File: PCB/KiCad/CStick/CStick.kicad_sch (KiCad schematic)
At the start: 6 parts, among them J1 Conn_01x04_Male, U1 Stickbox_Assembly

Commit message: 1.2.2 overhaul
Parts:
- added H5, H6: MouseBite, PhobGCC_Footprints:breakaway-mousebites-double, symbol Mechanical:MountingHole
- H1: footprint (none) -> PhobGCC_Footprints:MountingHole_1.8mm
- H2: footprint (none) -> PhobGCC_Footprints:MountingHole_5.2mm
- H3, H4: footprint (none) -> PhobGCC_Footprints:MountingHole_2.0mm
- U1: footprint (none) -> PhobGCC_Footprints:GCC_Stickbox_Hall_Only
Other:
- moved on the sheet: H1, H2, H3, H4, J1, U1

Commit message: Consolidated footprints to PhobGCC library
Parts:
- J1: footprint Connector_PinHeader_2.00mm:PinHeader_1x04_P2.00mm_Vertical -> (none)
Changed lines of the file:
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@@
     (property "Reference" "J1" (id 0) (at 44.577 32.2793 0))
     (property "Value" "Conn_01x04_Male" (id 1) (at 44.577 35.0544 0))
-    (property "Footprint" "Connector_PinHeader_2.00mm:PinHeader_1x04_P2.00mm_Vertical" (id 2) (at 43.942 38.862 0)
+    (property "Footprint" "" (id 2) (at 43.942 38.862 0)
       (effects (font (size 1.27 1.27)) hide)
     )
@@
     )
     (path "/61d7b681-5321-4eb3-aa94-2064a3bbd361"
-      (reference "J1") (unit 1) (value "Conn_01x04_Male") (footprint "Connector_PinHeader_2.00mm:PinHeader_1x04_P2.00mm_Vertical")
+      (reference "J1") (unit 1) (value "Conn_01x04_Male") (footprint "PhobGCC_Footprints:PinHeader_1x04_P2.00mm_Vertical")
     )
     (path "/8ae1c09a-53cf-4ff3-980c-45e96b7744a8"

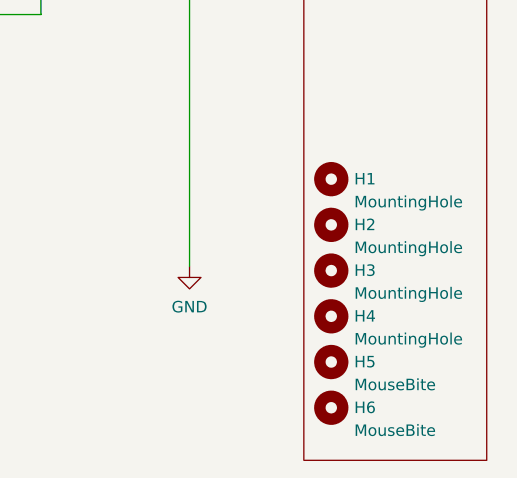
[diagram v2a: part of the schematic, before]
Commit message: 1.2.3 changes
omron tactile z support, larger c stick pin holes, relocated C10 from underneath button pad
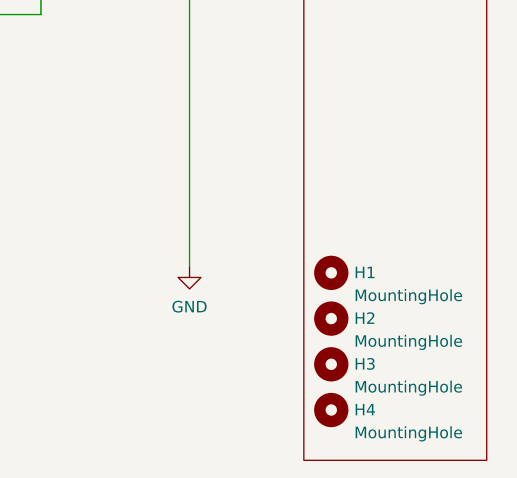
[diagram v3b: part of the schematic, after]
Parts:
- removed H5, H6: MouseBite, PhobGCC_Footprints:breakaway-mousebites-double, symbol Mechanical:MountingHole
- J1: footprint (none) -> PhobGCC_Footprints:PinHeader_1x04_P2.00mm_Vertical
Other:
- moved on the sheet: H1, H2, H3, H4
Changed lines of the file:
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@@
     (pin "1")
   )
-  (symbol (lib_id "Mechanical:MountingHole") (at 104.14 76.2 0) (unit 1)
+  (symbol (lib_id "Mechanical:MountingHole") (at 104.14 86.614 0) (unit 1)
     (in_bom yes) (on_board yes)
-    (property "Reference" "H3" (id 0) (at 106.68 76.2 0)
+    (property "Reference" "H3" (id 0) (at 106.68 86.614 0)
       (effects (font (size 1.27 1.27)) (justify left))
     )
-    (property "Value" "MountingHole" (id 1) (at 106.68 78.74 0)
+    (property "Value" "MountingHole" (id 1) (at 106.68 89.154 0)
       (effects (font (size 1.27 1.27)) (justify left))
     )
-    (property "Footprint" "PhobGCC_Footprints:MountingHole_2.0mm" (id 2) (at 104.14 76.2 0)
+    (property "Footprint" "PhobGCC_Footprints:MountingHole_2.0mm" (id 2) (at 104.14 86.614 0)
       (effects (font (size 1.27 1.27)) hide)
     )
-    (property "Datasheet" "~" (id 3) (at 104.14 76.2 0)
+    (property "Datasheet" "~" (id 3) (at 104.14 86.614 0)
       (effects (font (size 1.27 1.27)) hide)
     )
@@
     (pin "1")
   )
-  (symbol (lib_id "Mechanical:MountingHole") (at 104.14 81.28 0) (unit 1)
+  (symbol (lib_id "Mechanical:MountingHole") (at 104.14 91.694 0) (unit 1)
     (in_bom yes) (on_board yes)
-    (property "Reference" "H4" (id 0) (at 106.68 81.28 0)
+    (property "Reference" "H4" (id 0) (at 106.68 91.694 0)
       (effects (font (size 1.27 1.27)) (justify left))
     )
-    (property "Value" "MountingHole" (id 1) (at 106.68 83.82 0)
+    (property "Value" "MountingHole" (id 1) (at 106.68 94.234 0)
       (effects (font (size 1.27 1.27)) (justify left))
     )
-    (property "Footprint" "PhobGCC_Footprints:MountingHole_2.0mm" (id 2) (at 104.14 81.28 0)
+    (property "Footprint" "PhobGCC_Footprints:MountingHole_2.0mm" (id 2) (at 104.14 91.694 0)
       (effects (font (size 1.27 1.27)) hide)
     )
-    (property "Datasheet" "~" (id 3) (at 104.14 81.28 0)
+    (property "Datasheet" "~" (id 3) (at 104.14 91.694 0)
       (effects (font (size 1.27 1.27)) hide)
     )
@@
     (property "Reference" "J1" (id 0) (at 44.577 32.2793 0))
     (property "Value" "Conn_01x04_Male" (id 1) (at 44.577 35.0544 0))
-    (property "Footprint" "" (id 2) (at 43.942 38.862 0)
+    (property "Footprint" "PhobGCC_Footprints:PinHeader_1x04_P2.00mm_Vertical" (id 2) (at 43.942 38.862 0)
       (effects (font (size 1.27 1.27)) hide)
     )
@@
     (pin "1")
   )
-  (symbol (lib_id "Mechanical:MountingHole") (at 104.14 86.36 0) (unit 1)
+  (symbol (lib_id "Mechanical:MountingHole") (at 104.14 81.534 0) (unit 1)
     (in_bom yes) (on_board yes)
-    (property "Reference" "H5" (id 0) (at 106.68 86.36 0)
+    (property "Reference" "H2" (id 0) (at 106.68 81.534 0)
       (effects (font (size 1.27 1.27)) (justify left))
     )
-    (property "Value" "MouseBite" (id 1) (at 106.68 88.9 0)
+    (property "Value" "MountingHole" (id 1) (at 106.68 84.074 0)
       (effects (font (size 1.27 1.27)) (justify left))
     )
-    (property "Footprint" "PhobGCC_Footprints:breakaway-mousebites-double" (id 2) (at 104.14 86.36 0)
+    (property "Footprint" "PhobGCC_Footprints:MountingHole_5.2mm" (id 2) (at 104.14 81.534 0)
       (effects (font (size 1.27 1.27)) hide)
     )
-    (property "Datasheet" "~" (id 3) (at 104.14 86.36 0)
+    (property "Datasheet" "~" (id 3) (at 104.14 81.534 0)
       (effects (font (size 1.27 1.27)) hide)
     )
   )
-  (symbol (lib_id "Mechanical:MountingHole") (at 104.14 71.12 0) (unit 1)
+  (symbol (lib_id "Mechanical:MountingHole") (at 104.14 76.454 0) (unit 1)
     (in_bom yes) (on_board yes)
-    (property "Reference" "H2" (id 0) (at 106.68 71.12 0)
+    (property "Reference" "H1" (id 0) (at 106.68 76.454 0)
       (effects (font (size 1.27 1.27)) (justify left))
     )
-    (property "Value" "MountingHole" (id 1) (at 106.68 73.66 0)
+    (property "Value" "MountingHole" (id 1) (at 106.68 78.994 0)
       (effects (font (size 1.27 1.27)) (justify left))
     )
-    (property "Footprint" "PhobGCC_Footprints:MountingHole_5.2mm" (id 2) (at 104.14 71.12 0)
+    (property "Footprint" "PhobGCC_Footprints:MountingHole_1.8mm" (id 2) (at 104.14 76.454 0)
       (effects (font (size 1.27 1.27)) hide)
     )
-    (property "Datasheet" "~" (id 3) (at 104.14 71.12 0)
-      (effects (font (size 1.27 1.27)) hide)
-    )
-  )
-  (symbol (lib_id "Mechanical:MountingHole") (at 104.14 91.44 0) (unit 1)
-    (in_bom yes) (on_board yes)
-    (property "Reference" "H6" (id 0) (at 106.68 91.44 0)
-      (effects (font (size 1.27 1.27)) (justify left))
-    )
-    (property "Value" "MouseBite" (id 1) (at 106.68 93.98 0)
-      (effects (font (size 1.27 1.27)) (justify left))
-    )
-    (property "Footprint" "PhobGCC_Footprints:breakaway-mousebites-double" (id 2) (at 104.14 91.44 0)
-      (effects (font (size 1.27 1.27)) hide)
-    )
-    (property "Datasheet" "~" (id 3) (at 104.14 91.44 0)
-      (effects (font (size 1.27 1.27)) hide)
-    )
-  )
-  (symbol (lib_id "Mechanical:MountingHole") (at 104.14 66.04 0) (unit 1)
-    (in_bom yes) (on_board yes)
-    (property "Reference" "H1" (id 0) (at 106.68 66.04 0)
-      (effects (font (size 1.27 1.27)) (justify left))
-    )
-    (property "Value" "MountingHole" (id 1) (at 106.68 68.58 0)
-      (effects (font (size 1.27 1.27)) (justify left))
-    )
-    (property "Footprint" "PhobGCC_Footprints:MountingHole_1.8mm" (id 2) (at 104.14 66.04 0)
-      (effects (font (size 1.27 1.27)) hide)
-    )
-    (property "Datasheet" "~" (id 3) (at 104.14 66.04 0)
+    (property "Datasheet" "~" (id 3) (at 104.14 76.454 0)
       (effects (font (size 1.27 1.27)) hide)
     )
@@
       (reference "H4") (unit 1) (value "MountingHole") (footprint "PhobGCC_Footprints:MountingHole_2.0mm")
     )
-    (path "/b932399c-1e18-4768-a243-a3f6b8d2eaa5"
-      (reference "H5") (unit 1) (value "MouseBite") (footprint "PhobGCC_Footprints:breakaway-mousebites-double")
-    )
-    (path "/ce631169-40e5-44ad-95a8-46fd5f8c17a5"
-      (reference "H6") (unit 1) (value "MouseBite") (footprint "PhobGCC_Footprints:breakaway-mousebites-double")
-    )
     (path "/61d7b681-5321-4eb3-aa94-2064a3bbd361"
